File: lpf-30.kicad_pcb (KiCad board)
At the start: 2 copper layers, 76 x 20 mm, 23 parts

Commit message: improve lpf-30
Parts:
- removed M1, M2, M3, M4: , footprints:M3
- moved D1 0.10 mm to (144.0, 101.2)
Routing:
- net GND: track 9.10 -> 0.00 mm, vias 320 -> 411
- net FLT5: track 9.96 -> 8.96 mm
- net ATT1: track 8.70 -> 7.70 mm
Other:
- board size 76 x 20 mm -> 76 x 26 mm

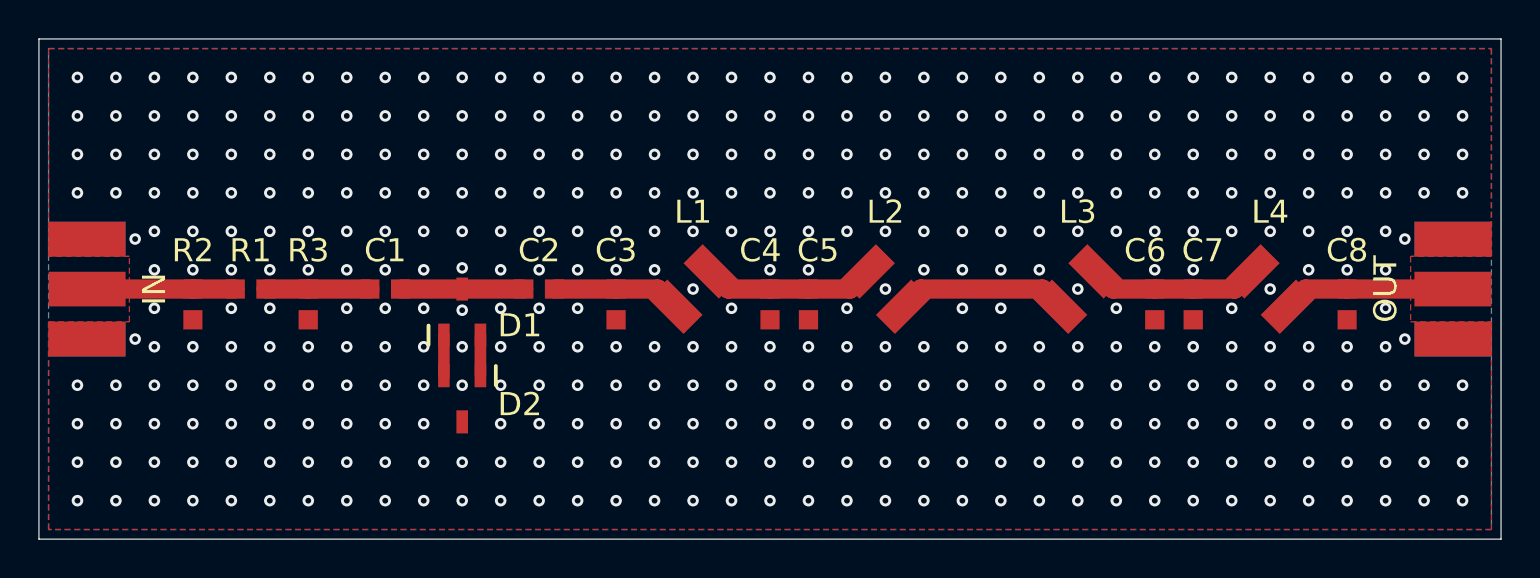
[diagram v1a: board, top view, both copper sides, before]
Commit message: replace 0603 with 0805 in lpf-30
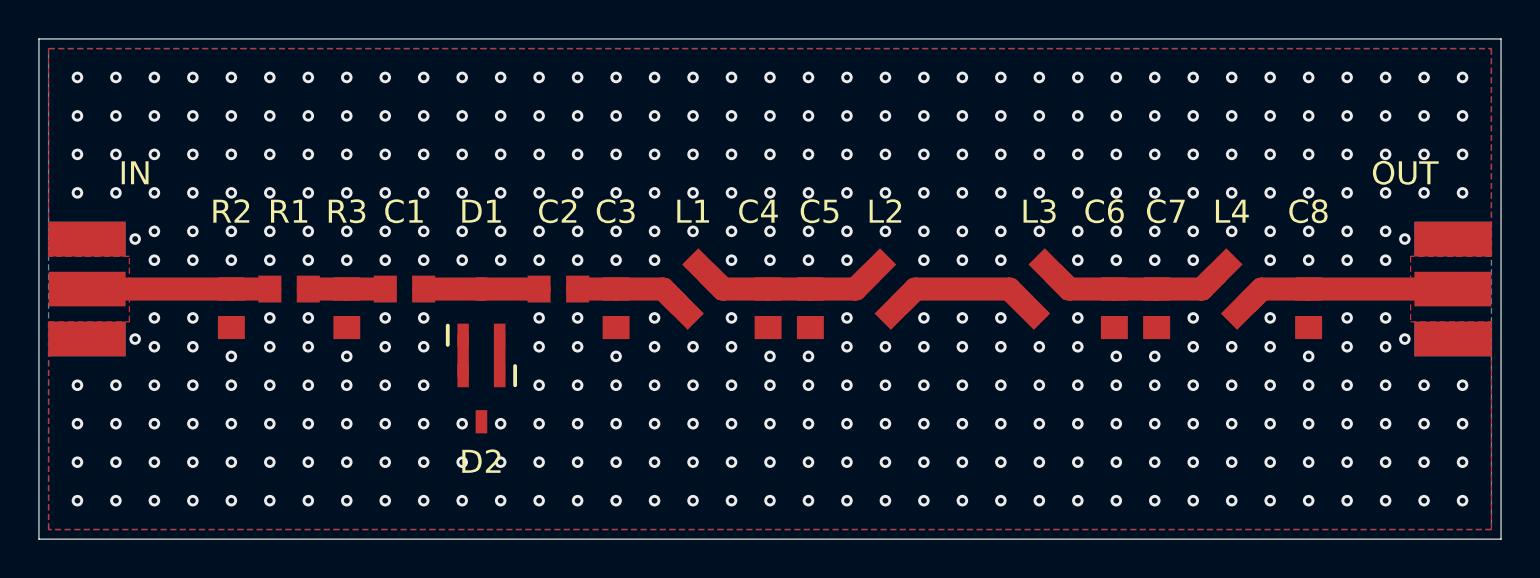
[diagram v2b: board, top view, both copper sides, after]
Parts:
- C1, C2, C3, C4, C5, C6, C7, C8, R1, R2, R3: footprint footprints:0603 -> footprints:0805
- moved C6 2.11 mm to (177.9, 101.0)
- moved C8 2.01 mm to (188.0, 101.0)
- moved R2 2.01 mm to (132.0, 101.0)
- moved R3 2.01 mm to (138.0, 101.0)
- moved L3 2.00 mm to (174.0, 100.0)
- moved L4 2.00 mm to (184.0, 100.0)
- moved R1 2.00 mm to (135.0, 100.0)
- moved C7 1.91 mm to (180.1, 101.0)
- moved C1 1.00 mm to (141.0, 100.0)
- moved C2 1.00 mm to (149.0, 100.0)
- moved D1 1.00 mm to (145.0, 101.2)
- moved D2 1.00 mm to (145.0, 105.7)
- moved C4 0.22 mm to (159.9, 101.0)
- moved C5 0.22 mm to (162.1, 101.0)
- moved C3 0.20 mm to (152.0, 101.0)
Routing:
- net FLT5: track 8.96 -> 11.0 mm
- net FLT3: track 8.92 -> 7.09 mm
- net ATT1: track 7.70 -> 9.50 mm
- net ATT2: track 5.40 -> 4.00 mm
- net FLT1: track 6.66 -> 5.54 mm
- net GND: vias 411 -> 410

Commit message: update SOT23-3 in lpf-30
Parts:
- turned D1 to -90 degrees
- turned D2 to 90 degrees
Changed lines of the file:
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@@
   )
   (footprint "footprints:SOT23-3" (layer "F.Cu")
-    (at 145 105.7 -90)
+    (at 145 105.7 90)
     (property "mpn" "C2500")
     (attr smd)
-    (fp_text reference "D2" (at 3.3 0) (layer "F.SilkS")
+    (fp_text reference "D2" (at -3.3 0) (layer "F.SilkS")
         (effects (font (size 1.2 1.2) (thickness 0.2)))
     )
@@
         (effects (font (size 1.27 1.27) (thickness 0.15)))
     )
-    (fp_text user "${REFERENCE}" (at 3.3 0) (layer "F.Fab")
-        (effects (font (size 1.2 1.2) (thickness 0.2)))
-    )
-    (fp_line (start -1.7 -1.75) (end -0.7 -1.75)
+    (fp_text user "${REFERENCE}" (at -3.3 0) (layer "F.Fab")
+        (effects (font (size 1.2 1.2) (thickness 0.2)))
+    )
+    (fp_line (start 0.7 1.75) (end 1.7 1.75)
       (stroke (width 0.2) (type solid)) (layer "F.SilkS"))
-    (pad "1" smd rect (at -1.2 -0.95) (size 0.6 1.2) (layers "F.Cu" "F.Paste" "F.Mask")
+    (pad "1" smd rect (at 1.2 0.95 180) (size 0.6 1.2) (layers "F.Cu" "F.Paste" "F.Mask")
       (net 1 "TVS3"))
-    (pad "2" smd rect (at -1.2 0.95) (size 0.6 1.2) (layers "F.Cu" "F.Paste" "F.Mask")
+    (pad "2" smd rect (at 1.2 -0.95 180) (size 0.6 1.2) (layers "F.Cu" "F.Paste" "F.Mask")
       (net 2 "TVS2"))
-    (pad "3" smd rect (at 1.2 0) (size 0.6 1.2) (layers "F.Cu" "F.Paste" "F.Mask")
+    (pad "3" smd rect (at -1.2 0 180) (size 0.6 1.2) (layers "F.Cu" "F.Paste" "F.Mask")
       (net 3 "GND"))
   )
@@
   )
   (footprint "footprints:SOT23-3" (layer "F.Cu")
-    (at 145 101.2 90)
+    (at 145 101.2 -90)
     (property "mpn" "C2500")
     (attr smd)
-    (fp_text reference "D1" (at 5.2 0 180) (layer "F.SilkS")
+    (fp_text reference "D1" (at -5.2 0) (layer "F.SilkS")
         (effects (font (size 1.2 1.2) (thickness 0.2)))
     )
@@
         (effects (font (size 1.27 1.27) (thickness 0.15)))
     )
-    (fp_text user "${REFERENCE}" (at 5.2 0 180) (layer "F.Fab")
-        (effects (font (size 1.2 1.2) (thickness 0.2)))
-    )
-    (fp_line (start -1.7 -1.75) (end -0.7 -1.75)
+    (fp_text user "${REFERENCE}" (at -5.2 0) (layer "F.Fab")
+        (effects (font (size 1.2 1.2) (thickness 0.2)))
+    )
+    (fp_line (start 0.7 1.75) (end 1.7 1.75)
       (stroke (width 0.2) (type solid)) (layer "F.SilkS"))
-    (pad "1" smd rect (at -1.2 -0.95 180) (size 0.6 1.2) (layers "F.Cu" "F.Paste" "F.Mask")
+    (pad "1" smd rect (at 1.2 0.95) (size 0.6 1.2) (layers "F.Cu" "F.Paste" "F.Mask")
       (net 2 "TVS2"))
-    (pad "2" smd rect (at -1.2 0.95 180) (size 0.6 1.2) (layers "F.Cu" "F.Paste" "F.Mask")
+    (pad "2" smd rect (at 1.2 -0.95) (size 0.6 1.2) (layers "F.Cu" "F.Paste" "F.Mask")
       (net 1 "TVS3"))
-    (pad "3" smd rect (at 1.2 0 180) (size 0.6 1.2) (layers "F.Cu" "F.Paste" "F.Mask")
+    (pad "3" smd rect (at -1.2 0) (size 0.6 1.2) (layers "F.Cu" "F.Paste" "F.Mask")
       (net 4 "TVS1"))
   )
